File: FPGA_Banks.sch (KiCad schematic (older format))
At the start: 36 parts

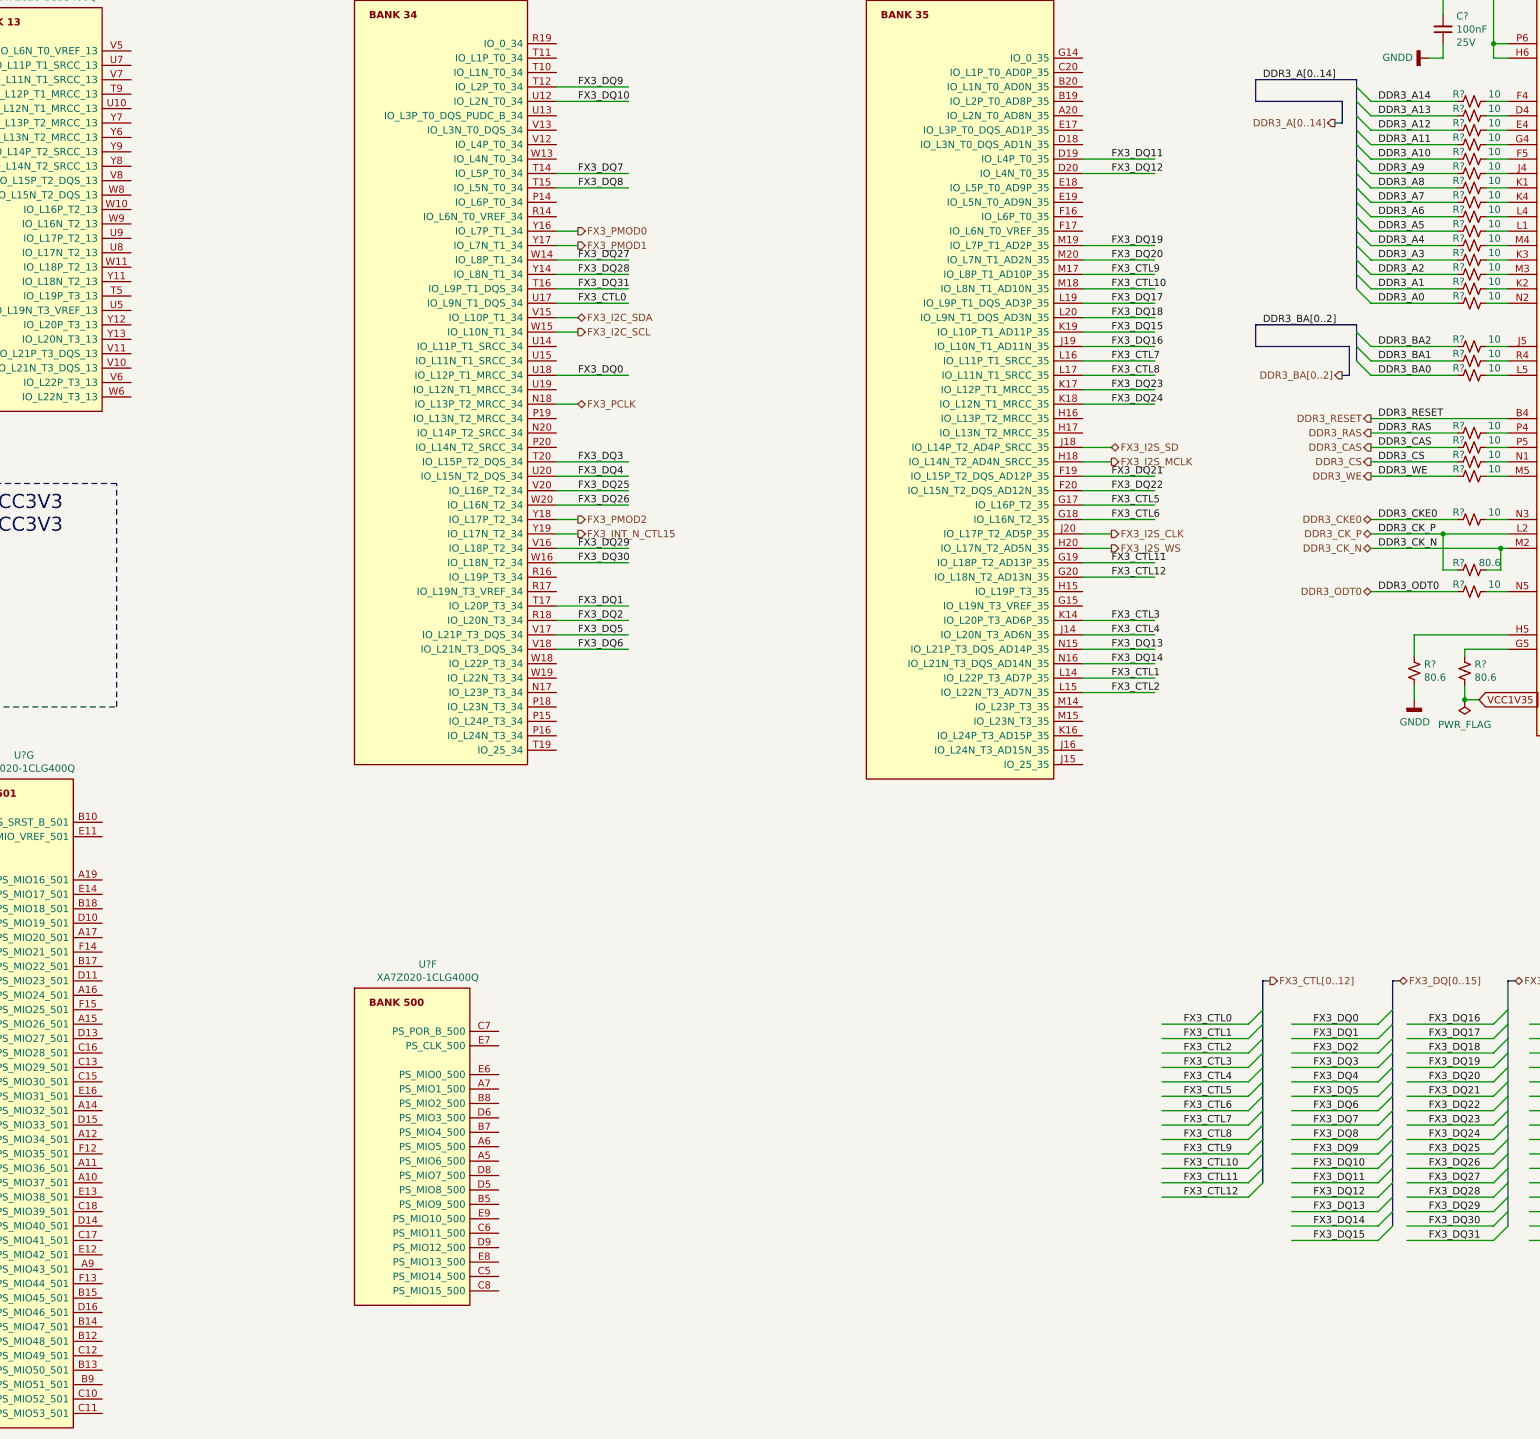
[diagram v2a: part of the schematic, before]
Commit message: Connected USB2 connections with FPGA and updated the top sheet
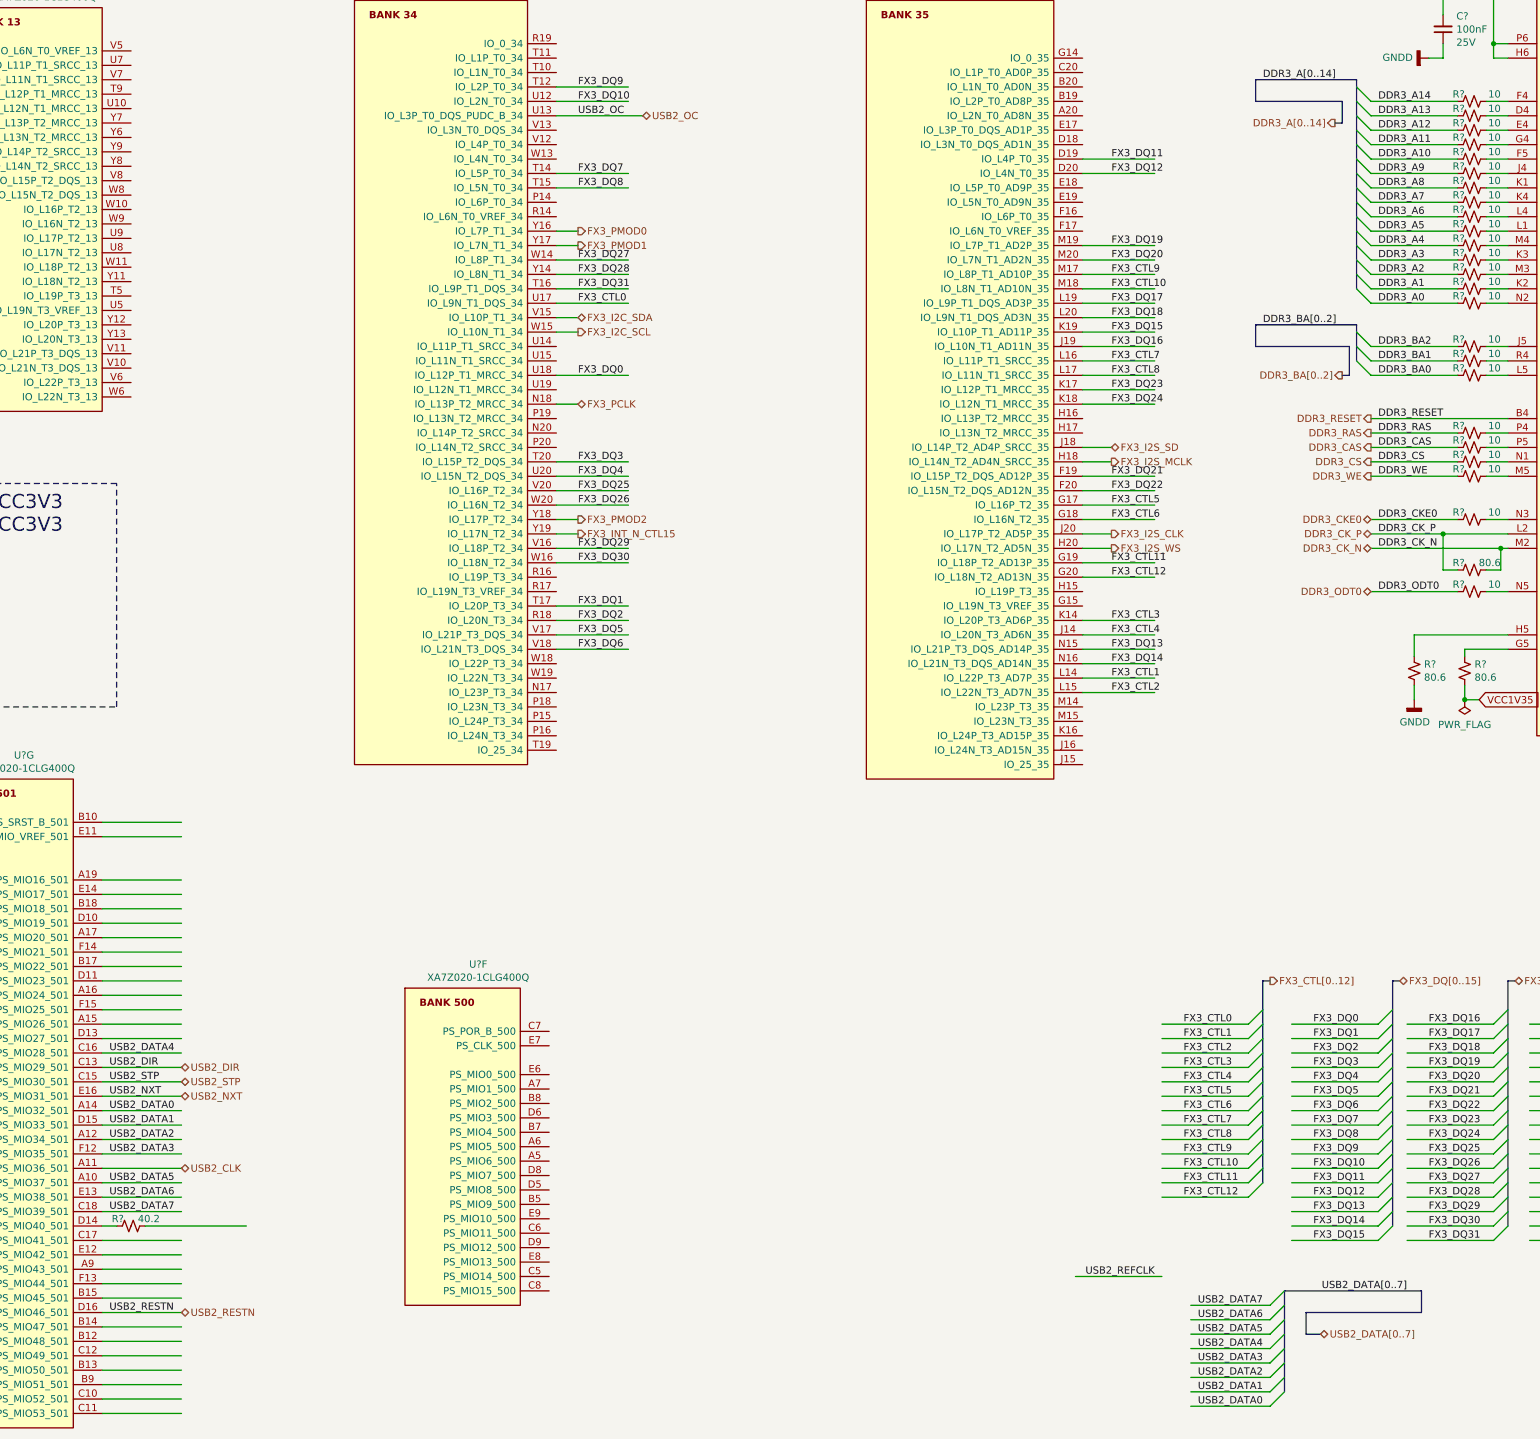
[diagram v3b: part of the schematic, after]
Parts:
- removed U?: XA7Z020-1CLG400Q, BGA400C80P20X20_1700X1700X160, symbol GM_FPGA:XA7Z020-1CLG400Q
- added R?: 40.2, Resistor_SMD:R_0201_0603Metric_Pad0.64x0.40mm_HandSolder, symbol Device:R_Small_US
- added U?: XA7Z020-1CLG400Q, BGA400C80P20X20_1700X1700X160, symbol GM_FPGA:XA7Z020-1CLG400Q
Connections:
- net labels added: USB2_CLK, USB2_DATA0, USB2_DATA1, USB2_DATA2, USB2_DATA3, USB2_DATA4, USB2_DATA5, USB2_DATA6, USB2_DATA7, USB2_DATA[0..7], USB2_DIR, USB2_NXT, USB2_OC, USB2_REFCLK, USB2_RESTN, USB2_STP
- wire segments 252 -> 303
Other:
- moved on the sheet: U?F
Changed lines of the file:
@@
 L GM_FPGA:XA7Z020-1CLG400Q U?
 U 6 1 604B00A9
-P 4250 7950
-F 0 "U?" H 4758 8115 50  0000 C CNN
-F 1 "XA7Z020-1CLG400Q" H 4758 8024 50  0000 C CNN
-F 2 "BGA400C80P20X20_1700X1700X160" H 7100 8050 50  0001 L CNN
-F 3 "http://www.xilinx.com/support/documentation/data_sheets/ds188-XA-Zynq-7000-Overview.pdf" H 7100 7950 50  0001 L CNN
-F 4 "XA7Z020-1CLG400Q" H 4250 7950 50  0001 C CNN "MPN"
-	6    4250 7950
-	1    0    0    -1
-$EndComp
-$Comp
-L GM_FPGA:XA7Z020-1CLG400Q U?
-U 7 1 604BC2A9
-P 1400 6500
-F 0 "U?" H 1958 6665 50  0000 C CNN
-F 1 "XA7Z020-1CLG400Q" H 1958 6574 50  0000 C CNN
-F 2 "BGA400C80P20X20_1700X1700X160" H 4250 6600 50  0001 L CNN
-F 3 "http://www.xilinx.com/support/documentation/data_sheets/ds188-XA-Zynq-7000-Overview.pdf" H 4250 6500 50  0001 L CNN
-F 4 "XA7Z020-1CLG400Q" H 1400 6500 50  0001 C CNN "MPN"
-	7    1400 6500
+P 4600 7950
+F 0 "U?" H 5108 8115 50  0000 C CNN
+F 1 "XA7Z020-1CLG400Q" H 5108 8024 50  0000 C CNN
+F 2 "BGA400C80P20X20_1700X1700X160" H 7450 8050 50  0001 L CNN
+F 3 "http://www.xilinx.com/support/documentation/data_sheets/ds188-XA-Zynq-7000-Overview.pdf" H 7450 7950 50  0001 L CNN
+F 4 "XA7Z020-1CLG400Q" H 4600 7950 50  0001 C CNN "MPN"
+	6    4600 7950
 	1    0    0    -1
 $EndComp
@@
 Wire Wire Line
 	5650 4800 5800 4800
+Text HLabel 10950 10350 2    50   BiDi ~ 0
+USB2_DATA[0..7]
+Text Label 10550 10750 2    50   ~ 0
+USB2_DATA1
+Text Label 10550 10650 2    50   ~ 0
+USB2_DATA2
+Text Label 10550 10550 2    50   ~ 0
+USB2_DATA3
+Text Label 10550 10450 2    50   ~ 0
+USB2_DATA4
+Text Label 10550 10350 2    50   ~ 0
+USB2_DATA5
+Text Label 10550 10250 2    50   ~ 0
+USB2_DATA6
+Text Label 10550 10150 2    50   ~ 0
+USB2_DATA7
+Text Label 10550 10850 2    50   ~ 0
+USB2_DATA0
+Text Label 9800 9950 2    50   ~ 0
+USB2_REFCLK
+Entry Wire Line
+	10700 10750 10600 10850
+Entry Wire Line
+	10700 10650 10600 10750
+Entry Wire Line
+	10700 10550 10600 10650
+Entry Wire Line
+	10700 10450 10600 10550
+Entry Wire Line
+	10700 10350 10600 10450
+Entry Wire Line
+	10700 10250 10600 10350
+Entry Wire Line
+	10700 10150 10600 10250
+Entry Wire Line
+	10700 10050 10600 10150
+Wire Bus Line
+	10700 10050 11650 10050
+Wire Bus Line
+	11650 10200 10850 10200
+Wire Bus Line
+	10850 10350 10950 10350
+Wire Bus Line
+	10850 10350 10850 10200
+Text Label 11550 10050 2    50   ~ 0
+USB2_DATA[0..7]
+Wire Wire Line
+	9250 9950 9850 9950
+Wire Wire Line
+	10600 10150 10050 10150
+Wire Wire Line
+	10600 10250 10050 10250
+Wire Wire Line
+	10600 10350 10050 10350
+Wire Wire Line
+	10600 10450 10050 10450
+Wire Wire Line
+	10600 10550 10050 10550
+Wire Wire Line
+	10600 10650 10050 10650
+Wire Wire Line
+	10600 10750 10050 10750
+Wire Wire Line
+	10600 10850 10050 10850
+Wire Bus Line
+	11650 10050 11650 10200
+Text Label 2550 8900 0    50   ~ 0
+USB2_DATA1
+Text Label 2550 9000 0    50   ~ 0
+USB2_DATA2
+Text Label 2550 9100 0    50   ~ 0
+USB2_DATA3
+Text Label 2550 8400 0    50   ~ 0
+USB2_DATA4
+Text Label 2550 9300 0    50   ~ 0
+USB2_DATA5
+Text Label 2550 9400 0    50   ~ 0
+USB2_DATA6
+Text Label 2550 9500 0    50   ~ 0
+USB2_DATA7
+Text Label 2550 8800 0    50   ~ 0
+USB2_DATA0
+Wire Wire Line
+	3050 9500 2500 9500
+Wire Wire Line
+	3050 9400 2500 9400
+Wire Wire Line
+	3050 9300 2500 9300
+Wire Wire Line
+	3050 9200 2500 9200
+Wire Wire Line
+	3050 9100 2500 9100
+Wire Wire Line
+	3050 9000 2500 9000
+Wire Wire Line
+	3050 8900 2500 8900
+Wire Wire Line
+	3050 8800 2500 8800
+$Comp
+L GM_FPGA:XA7Z020-1CLG400Q U?
+U 7 1 604FC306
+P 1400 6500
+F 0 "U?" H 1958 6665 50  0000 C CNN
+F 1 "XA7Z020-1CLG400Q" H 1958 6574 50  0000 C CNN
+F 2 "BGA400C80P20X20_1700X1700X160" H 4250 6600 50  0001 L CNN
+F 3 "http://www.xilinx.com/support/documentation/data_sheets/ds188-XA-Zynq-7000-Overview.pdf" H 4250 6500 50  0001 L CNN
+F 4 "XA7Z020-1CLG400Q" H 1400 6500 50  0001 C CNN "MPN"
+	7    1400 6500
+	1    0    0    -1
+$EndComp
+Wire Wire Line
+	3050 9900 2500 9900
+Wire Wire Line
+	3050 9800 2500 9800
+Wire Wire Line
+	3050 9700 2500 9700
+Wire Wire Line
+	3050 10300 2500 10300
+Wire Wire Line
+	3050 10200 2500 10200
+Wire Wire Line
+	3050 10100 2500 10100
+Wire Wire Line
+	3050 10000 2500 10000
+Wire Wire Line
+	3050 8700 2500 8700
+Wire Wire Line
+	3050 8600 2500 8600
+Wire Wire Line
+	3050 8500 2500 8500
+Wire Wire Line
+	3050 8400 2500 8400
+Wire Wire Line
+	3050 8300 2500 8300
+Wire Wire Line
+	3050 8200 2500 8200
+Wire Wire Line
+	3050 8100 2500 8100
+Wire Wire Line
+	3050 8000 2500 8000
+Wire Wire Line
+	3050 7900 2500 7900
+Wire Wire Line
+	3050 7800 2500 7800
+Wire Wire Line
+	3050 7700 2500 7700
+Wire Wire Line
+	3050 7600 2500 7600
+Wire Wire Line
+	3050 7500 2500 7500
+Wire Wire Line
+	3050 7400 2500 7400
+Wire Wire Line
+	3050 7300 2500 7300
+Wire Wire Line
+	3050 7200 2500 7200
+Wire Wire Line
+	3050 10700 2500 10700
+Wire Wire Line
+	3050 10600 2500 10600
+Wire Wire Line
+	3050 10500 2500 10500
+Wire Wire Line
+	3050 10400 2500 10400
+Wire Wire Line
+	3050 6900 2500 6900
+Wire Wire Line
+	3050 6800 2500 6800
+Wire Wire Line
+	3050 10900 2500 10900
+Wire Wire Line
+	3050 10800 2500 10800
+Text HLabel 3050 8500 2    50   BiDi ~ 0
+USB2_DIR
+Text HLabel 3050 8600 2    50   BiDi ~ 0
+USB2_STP
+Text HLabel 3050 8700 2    50   BiDi ~ 0
+USB2_NXT
+Text Label 2550 8500 0    50   ~ 0
+USB2_DIR
+Text Label 2550 8600 0    50   ~ 0
+USB2_STP
+Text Label 2550 8700 0    50   ~ 0
+USB2_NXT
+Text Label 2550 10200 0    50   ~ 0
+USB2_RESTN
+Text HLabel 3050 9200 2    50   BiDi ~ 0
+USB2_CLK
+Text HLabel 3050 10200 2    50   BiDi ~ 0
+USB2_RESTN
+$Comp
+L Device:R_Small_US R?
+U 1 1 60927F13
+P 2700 9600
+AR Path="/601E7C5A/60927F13" Ref="R?"  Part="1"
+AR Path="/601E7CC8/60927F13" Ref="R?"  Part="1"
+AR Path="/601E7C92/60927F13" Ref="R?"  Part="1"
+AR Path="/601E7C92/60257FE5/60927F13" Ref="R?"  Part="1"
+AR Path="/601E7B38/60927F13" Ref="R?"  Part="1"
+AR Path="/601E7BF0/60927F13" Ref="R?"  Part="1"
+AR Path="/60391560/60927F13" Ref="R?"  Part="1"
+AR Path="/6041EB92/60927F13" Ref="R?"  Part="1"
+F 0 "R?" V 2750 9650 50  0000 L CNN
+F 1 "40.2" V 2750 9400 50  0000 L CNN
+F 2 "Resistor_SMD:R_0201_0603Metric_Pad0.64x0.40mm_HandSolder" H 2700 9600 50  0001 C CNN
+F 3 "~" H 2700 9600 50  0001 C CNN
+	1    2700 9600
+	0    -1   -1   0
+$EndComp
+Wire Wire Line
+	2500 9600 2600 9600
+Wire Wire Line
+	2800 9600 3500 9600
+Text HLabel 6250 1900 2    50   BiDi ~ 0
+USB2_OC
+Text Label 5800 1900 0    50   ~ 0
+USB2_OC
+Wire Wire Line
+	6250 1900 5650 1900
 Wire Bus Line
 	11200 3350 11200 3600
 Wire Bus Line
+	10700 10050 10700 10750
+Wire Bus Line
 	11200 1650 11200 3100
